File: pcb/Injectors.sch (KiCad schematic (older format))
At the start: 55 parts, among them Q1 VND14NV04, Q2 VND14NV04, Q3 VND14NV04, Q4 VND14NV04, Q5 VND14NV04, Q6 VND14NV04, Q7 VND14NV04, Q8 VND14NV04

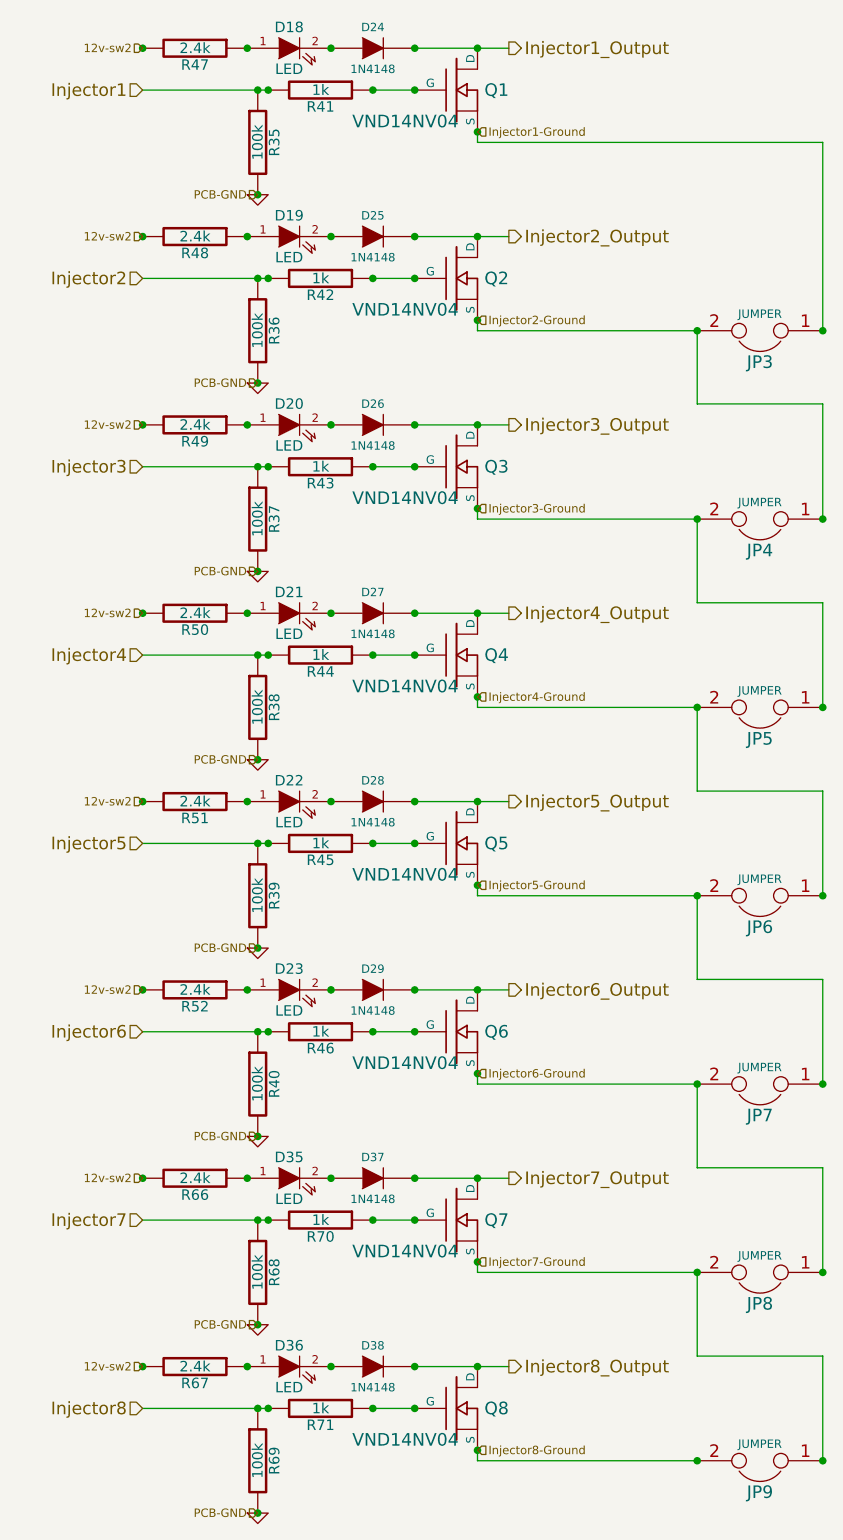
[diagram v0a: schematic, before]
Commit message: Changed 2.4k ohm resistor to 2.43k ohm resistor due to physical size issue.
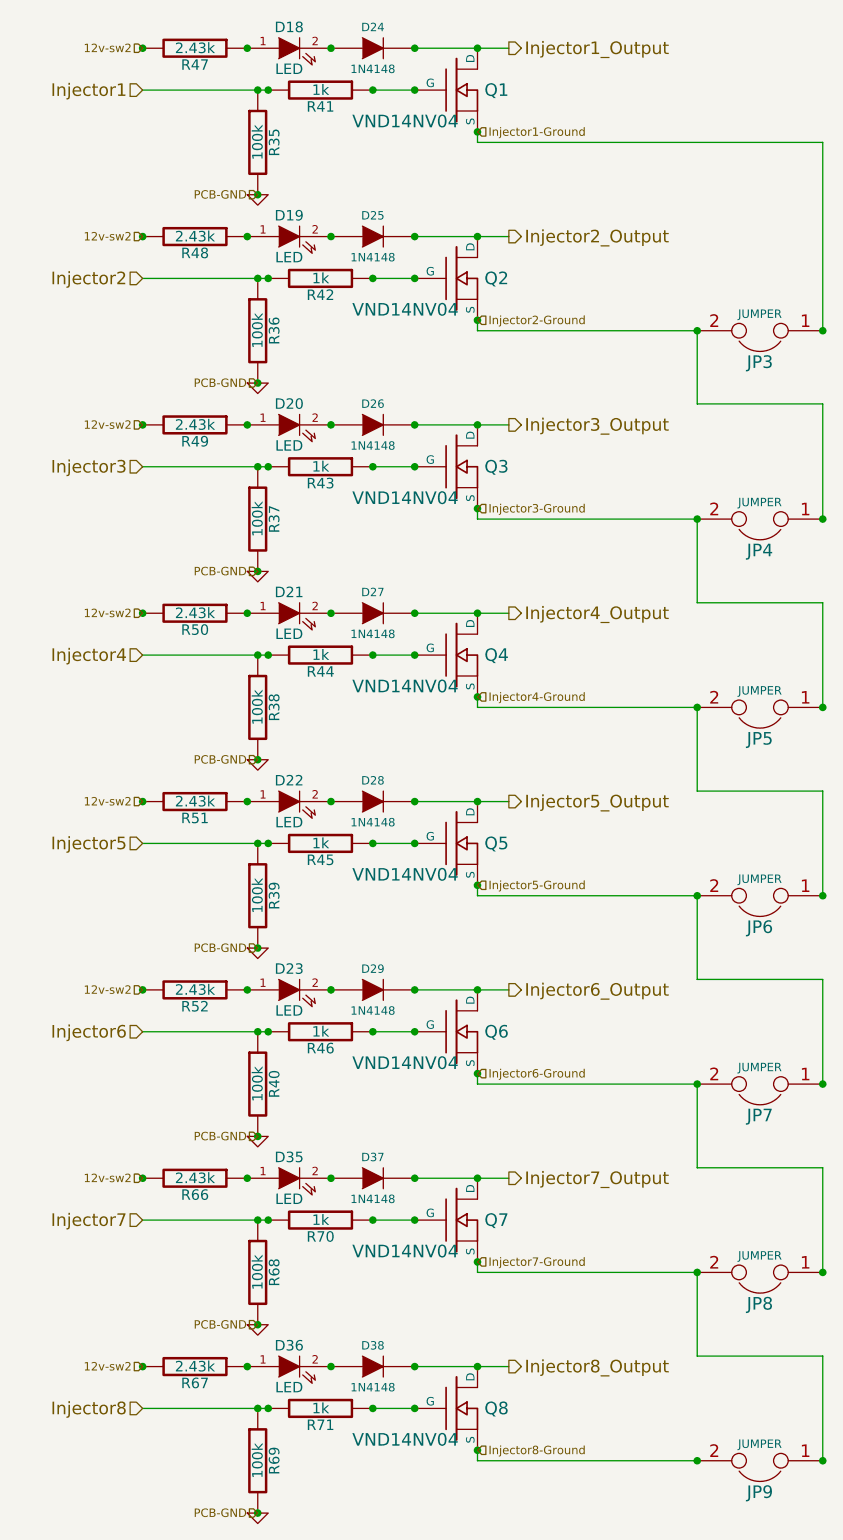
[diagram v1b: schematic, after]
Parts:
- R47, R48, R49, R50, R51, R52, R66, R67: value 2.4k -> 2.43k

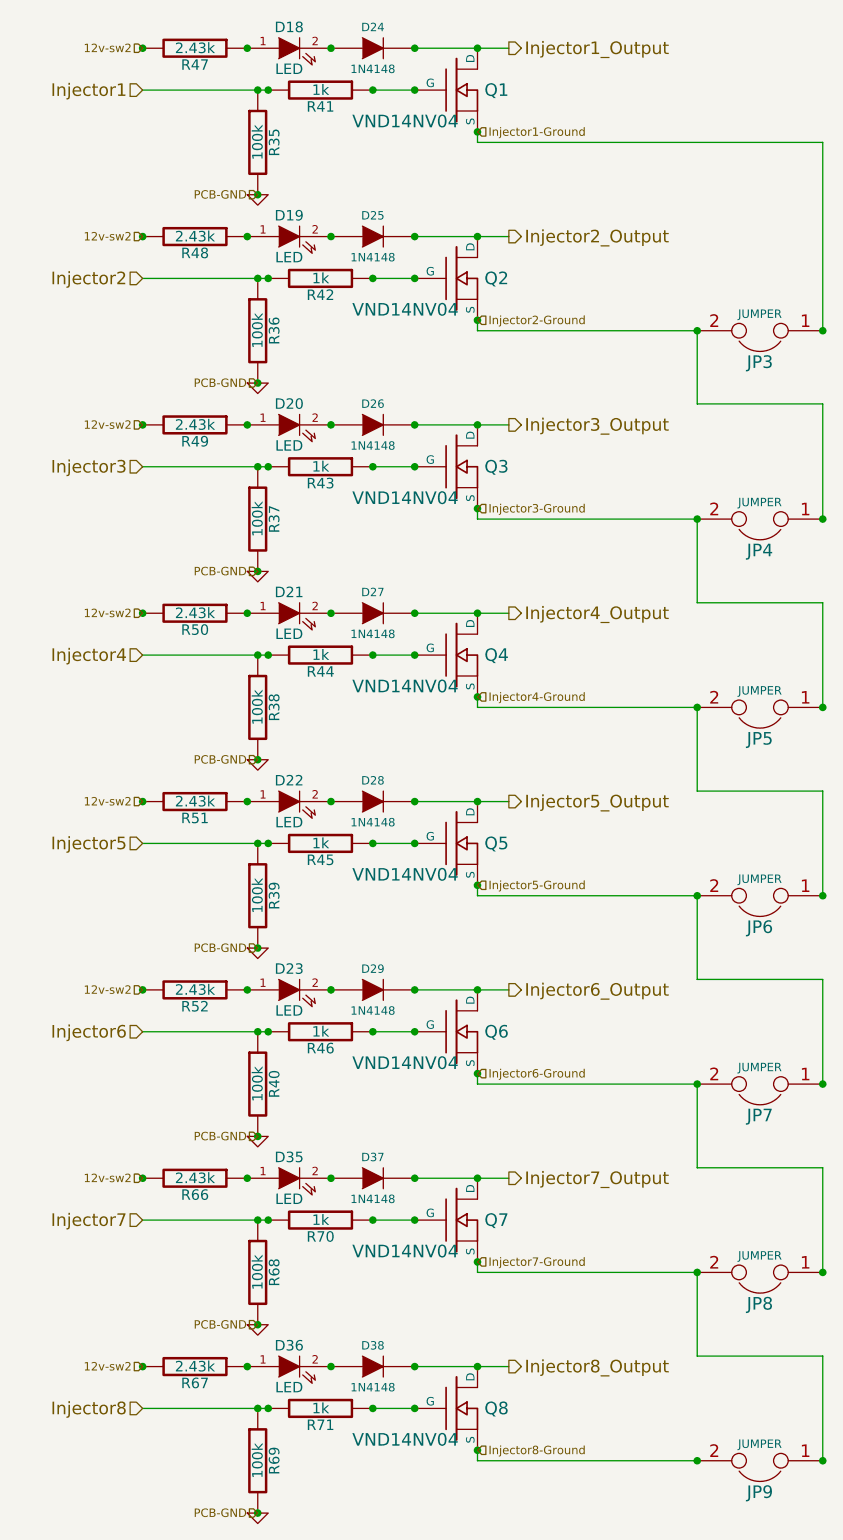
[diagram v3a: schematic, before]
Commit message: Added LEDs and resistors to ignitor outputs.
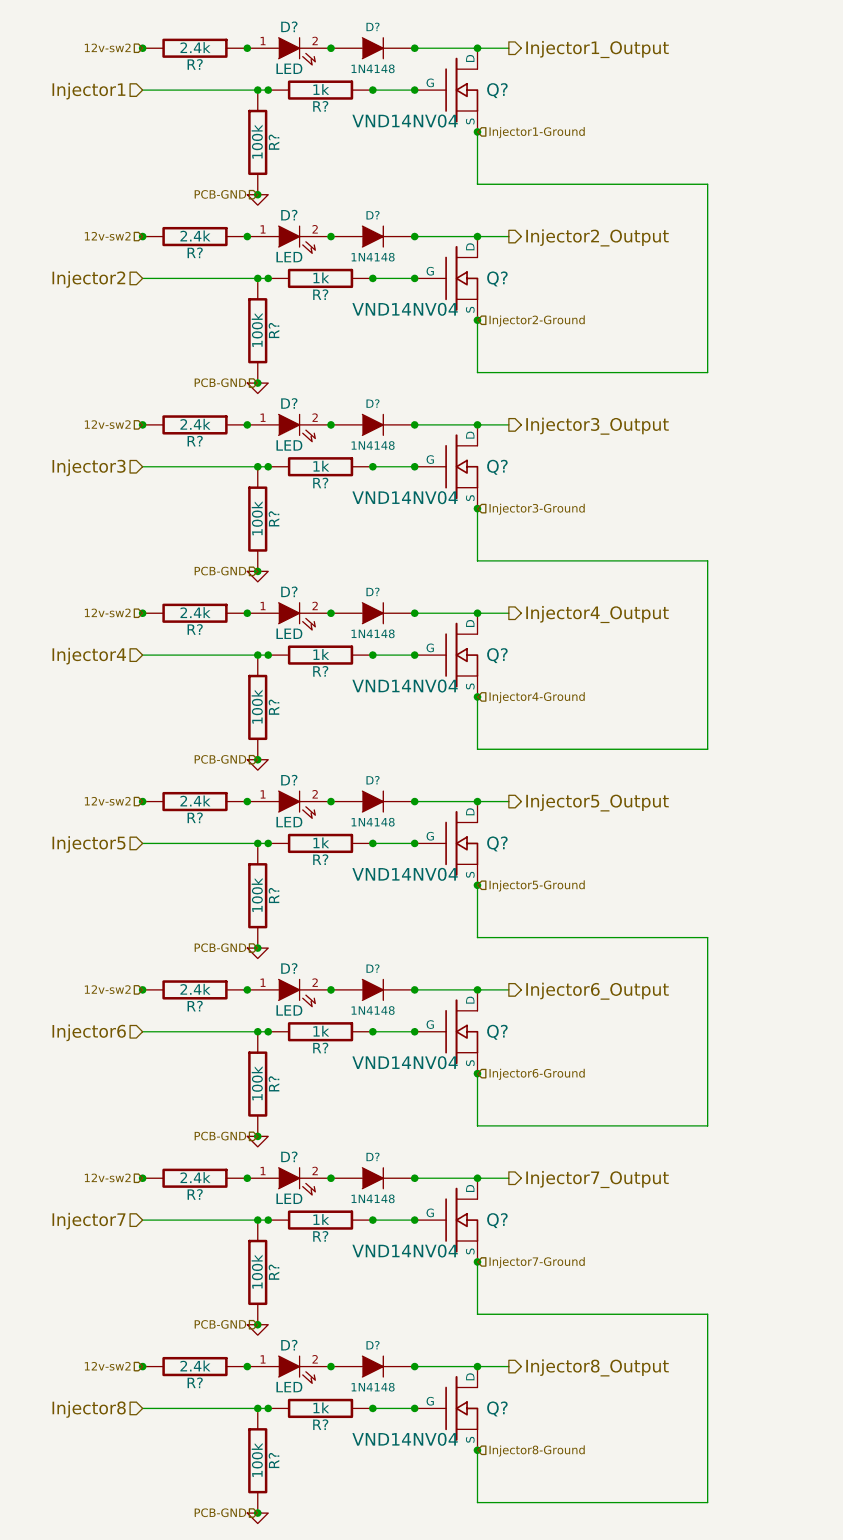
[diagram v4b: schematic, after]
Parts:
- removed JP3, JP4, JP5, JP6, JP7, JP8, JP9: JUMPER, symbol JUMPER
- R?: renamed from R47; value 2.43k -> 2.4k
- R?: renamed from R48; value 2.43k -> 2.4k
- R?: renamed from R49; value 2.43k -> 2.4k
- R?: renamed from R50; value 2.43k -> 2.4k
- R?: renamed from R51; value 2.43k -> 2.4k
- R?: renamed from R52; value 2.43k -> 2.4k
- R?: renamed from R66; value 2.43k -> 2.4k
- R?: renamed from R67; value 2.43k -> 2.4k
- renumbered D18 to D?, D19 to D?, D20 to D?, D21 to D?, D22 to D?, D23 to D?, D24 to D?, D25 to D?, D26 to D?, D27 to D?, D28 to D?, D29 to D?, D37 to D?, D35 to D?, D36 to D?, D38 to D?, Q1 to Q?, Q2 to Q?, Q3 to Q?, Q4 to Q?, Q5 to Q?, Q6 to Q?, Q7 to Q?, Q8 to Q?, R35 to R?, R41 to R?, R42 to R?, R36 to R?, R43 to R?, R37 to R?, R44 to R?, R38 to R?, R39 to R?, R45 to R?, R46 to R?, R40 to R?, R68 to R?, R70 to R?, R71 to R?, R69 to R?
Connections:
- net Injector2-Ground is gone; now on net Injector1-Ground: Q?.S
- net Injector4-Ground is gone; now on net Injector3-Ground: Q?.S
- net Injector6-Ground is gone; now on net Injector5-Ground: Q?.S
- net Injector8-Ground is gone; now on net Injector7-Ground: Q?.S

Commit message: Changed revision to 0.7-alpha and git hash to xxxxxxxxxx to show that this is in progress.
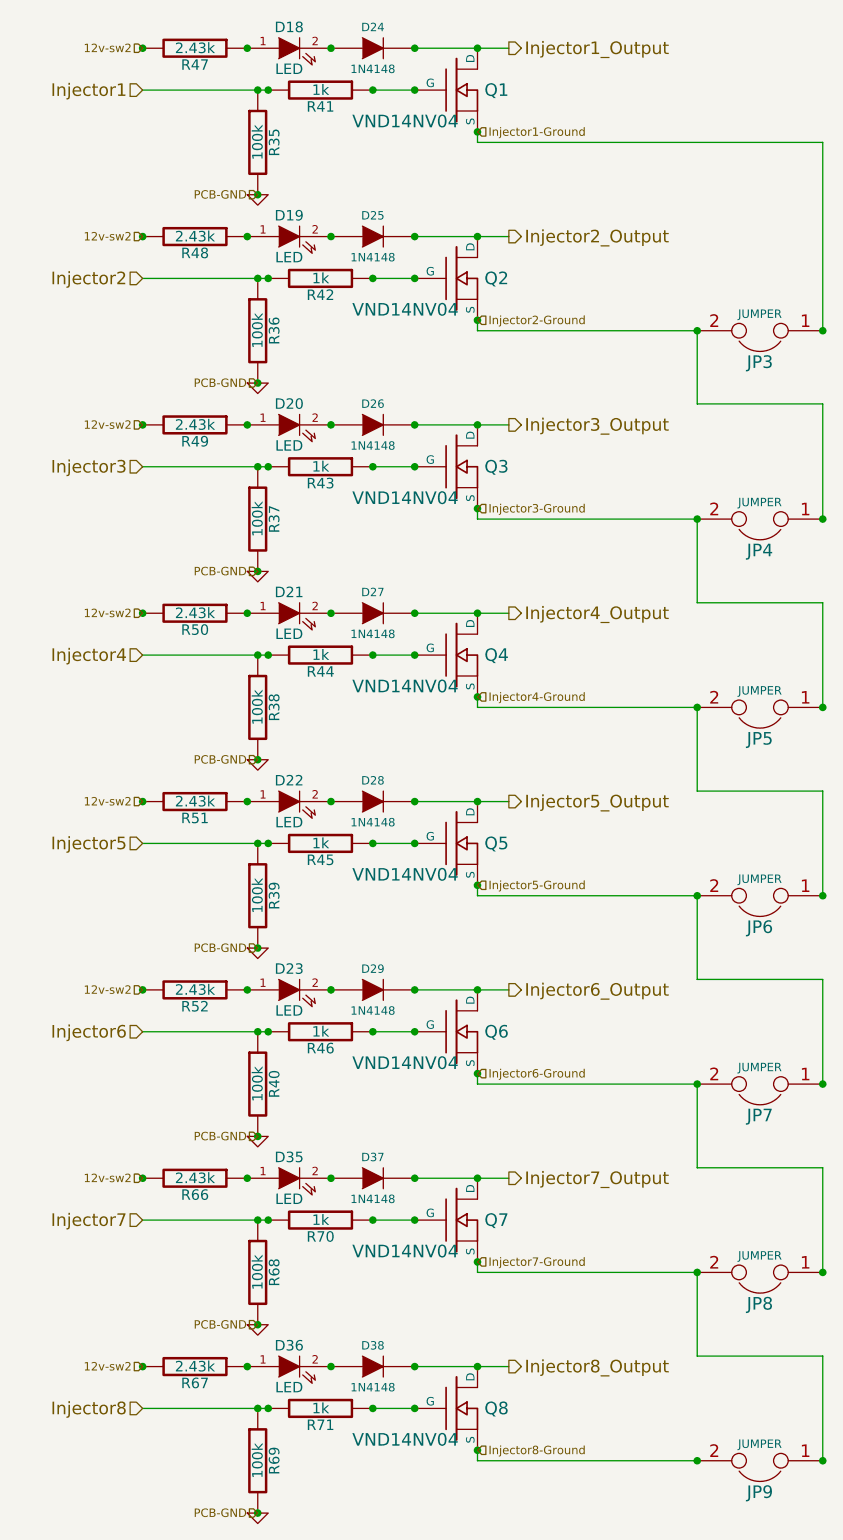
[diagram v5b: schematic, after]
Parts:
- added JP3, JP4, JP5, JP6, JP7, JP8, JP9: JUMPER, symbol JUMPER
- R47, R48, R49, R50, R51, R52, R66, R67: renamed from R?; value 2.4k -> 2.43k
- gave numbers to parts that had none: 40
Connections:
- net Injector1-Ground: now also JP3.1; no longer Q2.S
- net Injector3-Ground: now also JP4.2, JP5.1; no longer Q4.S
- net Injector5-Ground: now also JP6.2, JP7.1; no longer Q6.S
- net Injector7-Ground: now also JP8.2, JP9.1; no longer Q8.S
- new net Injector2-Ground: JP3.2, JP4.1, Q2.S
- new net Injector4-Ground: JP5.2, JP6.1, Q4.S
- new net Injector6-Ground: JP7.2, JP8.1, Q6.S
- new net Injector8-Ground: JP9.2, Q8.S
